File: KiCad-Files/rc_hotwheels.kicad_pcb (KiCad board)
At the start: 2 copper layers, 29.5 x 21.6 mm, 16 parts, among them IC1 BD6211F-E2, IC2 MIC5504-3.3YM5-TR, M1 Motor_Connection, U1 STM32F070F6P6, U3 NRF24L01_Breakout

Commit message: Merge branch 'master' of https://github.com/404boboo/RC-Hotwheels
Small changes in tracing
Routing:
- net Motor Speed: track 24.7 -> 24.2 mm
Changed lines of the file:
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@@
   (segment (start 61.39392 36.997797) (end 61.39392 39.72348) (width 0.4) (layer "F.Cu") (net 2))
   (segment (start 63.627 43.8856) (end 61.6458 43.8856) (width 0.4) (layer "F.Cu") (net 2))
+  (segment (start 62.743879 51.2262) (end 64.4906 51.2262) (width 0.4) (layer "F.Cu") (net 2))
   (segment (start 76.1238 35.2298) (end 71.058328 40.295272) (width 0.4) (layer "F.Cu") (net 2))
+  (segment (start 61.976 50.458321) (end 62.743879 51.2262) (width 0.4) (layer "F.Cu") (net 2))
   (segment (start 73.981636 48.110564) (end 76.7588 45.3334) (width 0.4) (layer "F.Cu") (net 2))
-  (segment (start 60.2742 44.7548) (end 61.4934 45.974) (width 0.4) (layer "F.Cu") (net 2))
+  (segment (start 61.976 46.4566) (end 61.976 50.458321) (width 0.4) (layer "F.Cu") (net 2))
   (segment (start 66.081593 44.170272) (end 63.911672 44.170272) (width 0.4) (layer "F.Cu") (net 2))
+  (segment (start 60.2742 44.7548) (end 61.976 46.4566) (width 0.4) (layer "F.Cu") (net 2))
   (segment (start 61.6458 43.8856) (end 60.3306 43.8856) (width 0.4) (layer "F.Cu") (net 2))
-  (segment (start 61.976 50.458321) (end 61.976 46.8122) (width 0.4) (layer "F.Cu") (net 2))
   (segment (start 64.4906 51.2262) (end 66.5378 51.2262) (width 0.4) (layer "F.Cu") (net 2))
   (segment (start 76.5048 35.2298) (end 76.1238 35.2298) (width 0.4) (layer "F.Cu") (net 2))
@@
   (segment (start 74.803 45.3334) (end 76.7588 45.3334) (width 0.4) (layer "F.Cu") (net 2))
   (segment (start 62.004364 48.110564) (end 73.981636 48.110564) (width 0.4) (layer "F.Cu") (net 2))
-  (segment (start 61.4934 45.974) (end 61.976 45.974) (width 0.4) (layer "F.Cu") (net 2))
   (segment (start 61.39392 39.72348) (end 60.2742 40.8432) (width 0.4) (layer "F.Cu") (net 2))
-  (segment (start 61.976 46.8122) (end 61.976 45.974) (width 0.4) (layer "F.Cu") (net 2))
   (segment (start 70.06 41.289679) (end 70.06 44.100544) (width 0.4) (layer "F.Cu") (net 2))
   (segment (start 69.990272 44.170272) (end 66.081593 44.170272) (width 0.4) (layer "F.Cu") (net 2))
@@
   (segment (start 71.054407 40.295272) (end 70.06 41.289679) (width 0.4) (layer "F.Cu") (net 2))
   (segment (start 63.911672 44.170272) (end 63.627 43.8856) (width 0.4) (layer "F.Cu") (net 2))
-  (segment (start 62.743879 51.2262) (end 61.976 50.458321) (width 0.4) (layer "F.Cu") (net 2))
-  (segment (start 64.4906 51.2262) (end 62.743879 51.2262) (width 0.4) (layer "F.Cu") (net 2))
   (segment (start 60.3306 43.8856) (end 60.2742 43.942) (width 0.4) (layer "F.Cu") (net 2))
   (segment (start 66.5378 51.2262) (end 66.588 51.176) (width 0.4) (layer "F.Cu") (net 2))
@@
   (segment (start 66.081593 39.14547) (end 66.081593 40.920272) (width 0.2) (layer "F.Cu") (net 13))
   (segment (start 65.22392 38.287797) (end 66.081593 39.14547) (width 0.2) (layer "F.Cu") (net 13))
+  (segment (start 67.76392 41.383102) (end 67.76392 38.287797) (width 0.2) (layer "F.Cu") (net 14))
+  (segment (start 67.57675 41.570272) (end 67.76392 41.383102) (width 0.2) (layer "F.Cu") (net 14))
   (segment (start 66.081593 41.570272) (end 67.57675 41.570272) (width 0.2) (layer "F.Cu") (net 14))
-  (segment (start 67.57675 41.570272) (end 67.76392 41.383102) (width 0.2) (layer "F.Cu") (net 14))
-  (segment (start 67.76392 41.383102) (end 67.76392 38.287797) (width 0.2) (layer "F.Cu") (net 14))
   (segment (start 65.044093 41.015693) (end 65.044093 41.919536) (width 0.2) (layer "F.Cu") (net 15))
   (segment (start 65.344829 42.220272) (end 66.081593 42.220272) (width 0.2) (layer "F.Cu") (net 15))
@@
   (segment (start 65.22392 35.747797) (end 64.008 36.963717) (width 0.2) (layer "F.Cu") (net 15))
   (segment (start 65.044093 41.919536) (end 65.344829 42.220272) (width 0.2) (layer "F.Cu") (net 15))
-  (segment (start 68.355529 42.19) (end 67.845529 42.7) (width 0.2) (layer "F.Cu") (net 18))
-  (segment (start 71.4248 37.96788) (end 68.355529 41.037151) (width 0.2) (layer "F.Cu") (net 18))
+  (segment (start 68.8605 41.685029) (end 67.845529 42.7) (width 0.2) (layer "F.Cu") (net 18))
+  (segment (start 68.8605 40.532181) (end 68.8605 41.685029) (width 0.2) (layer "F.Cu") (net 18))
+  (segment (start 71.4248 37.96788) (end 68.8605 40.532181) (width 0.2) (layer "F.Cu") (net 18))
+  (segment (start 68.289728 46.120272) (end 66.081593 46.120272) (width 0.2) (layer "F.Cu") (net 18))
+  (segment (start 71.4248 35.2298) (end 71.4248 37.96788) (width 0.2) (layer "F.Cu") (net 18))
   (segment (start 67.845529 42.7) (end 67.8 42.7) (width 0.2) (layer "F.Cu") (net 18))
-  (segment (start 68.289728 46.120272) (end 66.081593 46.120272) (width 0.2) (layer "F.Cu") (net 18))
-  (segment (start 68.355529 41.037151) (end 68.355529 42.19) (width 0.2) (layer "F.Cu") (net 18))
   (segment (start 68.72 45.69) (end 68.289728 46.120272) (width 0.2) (layer "F.Cu") (net 18))
-  (segment (start 71.4248 35.2298) (end 71.4248 37.96788) (width 0.2) (layer "F.Cu") (net 18))
   (via (at 68.72 45.69) (size 0.8) (drill 0.4) (layers "F.Cu" "B.Cu") (net 18))
   (via (at 67.8 42.7) (size 0.8) (drill 0.4) (layers "F.Cu" "B.Cu") (net 18))
@@
   (segment (start 67.8 42.7) (end 67.8 44.77) (width 0.2) (layer "B.Cu") (net 18))
   (segment (start 73.9648 35.2298) (end 73.9648 35.993566) (width 0.2) (layer "F.Cu") (net 19))
-  (segment (start 73.9648 35.993566) (end 68.755529 41.202837) (width 0.2) (layer "F.Cu") (net 19))
-  (segment (start 68.755529 41.202837) (end 68.755529 42.364471) (width 0.2) (layer "F.Cu") (net 19))
+  (segment (start 73.9648 35.993566) (end 69.2605 40.697866) (width 0.2) (layer "F.Cu") (net 19))
   (segment (start 69.219728 46.770272) (end 66.081593 46.770272) (width 0.2) (layer "F.Cu") (net 19))
-  (segment (start 68.755529 42.364471) (end 69.231058 42.84) (width 0.2) (layer "F.Cu") (net 19))
-  (segment (start 69.231058 42.84) (end 69.2605 42.84) (width 0.2) (layer "F.Cu") (net 19))
+  (segment (start 69.2605 40.697866) (end 69.2605 42.84) (width 0.2) (layer "F.Cu") (net 19))
   (segment (start 69.71 46.28) (end 69.219728 46.770272) (width 0.2) (layer "F.Cu") (net 19))
   (via (at 69.71 46.28) (size 0.8) (drill 0.4) (layers "F.Cu" "B.Cu") (net 19))
@@
   (segment (start 65.202951 54.5338) (end 60.046751 49.3776) (width 0.4) (layer "F.Cu") (net 20))
   (segment (start 70.9422 51.658) (end 70.9422 54.356) (width 0.4) (layer "F.Cu") (net 20))
+  (segment (start 77.948391 37.901009) (end 77.948391 51.369988) (width 0.4) (layer "F.Cu") (net 20))
   (segment (start 81.8896 38.6842) (end 81.8896 37.2618) (width 0.4) (layer "F.Cu") (net 20))
   (segment (start 81.7372 37.1094) (end 79.7198 37.1094) (width 0.4) (layer "F.Cu") (net 20))
   (segment (start 76.246392 54.5338) (end 71.12 54.5338) (width 0.4) (layer "F.Cu") (net 20))
-  (segment (start 79.7198 37.1094) (end 78.045782 37.1094) (width 0.4) (layer "F.Cu") (net 20))
-  (segment (start 78.045782 37.1094) (end 77.948391 37.206791) (width 0.4) (layer "F.Cu") (net 20))
   (segment (start 77.443517 53.336675) (end 76.246392 54.5338) (width 0.4) (layer "F.Cu") (net 20))
   (segment (start 69.088 51.176) (end 70.4602 51.176) (width 0.4) (layer "F.Cu") (net 20))
-  (segment (start 77.443517 51.874862) (end 77.948391 51.369988) (width 0.4) (layer "F.Cu") (net 20))
   (segment (start 81.8896 37.2618) (end 81.7372 37.1094) (width 0.4) (layer "F.Cu") (net 20))
   (segment (start 79.7198 37.1094) (end 80.6196 38.0092) (width 0.4) (layer "F.Cu") (net 20))
@@
   (segment (start 77.443517 51.874862) (end 77.443517 53.336675) (width 0.4) (layer "F.Cu") (net 20))
   (segment (start 60.046751 49.3776) (end 59.7916 49.3776) (width 0.4) (layer "F.Cu") (net 20))
-  (segment (start 77.948391 37.206791) (end 77.948391 51.369988) (width 0.4) (layer "F.Cu") (net 20))
+  (segment (start 77.948391 51.369988) (end 77.443517 51.874862) (width 0.4) (layer "F.Cu") (net 20))
+  (segment (start 78.74 37.1094) (end 77.948391 37.901009) (width 0.4) (layer "F.Cu") (net 20))
   (segment (start 70.9422 54.356) (end 71.12 54.5338) (width 0.4) (layer "F.Cu") (net 20))
+  (segment (start 79.7198 37.1094) (end 78.74 37.1094) (width 0.4) (layer "F.Cu") (net 20))
   (segment (start 80.6196 38.0092) (end 80.6196 38.6842) (width 0.4) (layer "F.Cu") (net 20))
   (segment (start 71.12 54.5338) (end 65.202951 54.5338) (width 0.4) (layer "F.Cu") (net 20))
@@
   (segment (start 76.806344 41.613585) (end 79.108428 41.613585) (width 0.2) (layer "B.Cu") (net 23))
   (segment (start 76.247654 41.054895) (end 76.806344 41.613585) (width 0.2) (layer "B.Cu") (net 23))
-  (segment (start 63.5 46.736) (end 63.5 45.490695) (width 0.2) (layer "F.Cu") (net 24))
-  (segment (start 63.585989 45.404706) (end 64.216575 45.404706) (width 0.2) (layer "F.Cu") (net 24))
+  (segment (start 65.116303 44.820272) (end 66.081593 44.820272) (width 0.2) (layer "F.Cu") (net 24))
+  (segment (start 63.5 46.736) (end 63.5 46.436575) (width 0.2) (layer "F.Cu") (net 24))
   (segment (start 80.6196 47.5742) (end 80.6196 44.5842) (width 0.2) (layer "F.Cu") (net 24))
-  (segment (start 64.216575 45.404706) (end 64.801009 44.820272) (width 0.2) (layer "F.Cu") (net 24))
-  (segment (start 64.801009 44.820272) (end 66.081593 44.820272) (width 0.2) (layer "F.Cu") (net 24))
-  (segment (start 63.5 45.490695) (end 63.585989 45.404706) (width 0.2) (layer "F.Cu") (net 24))
+  (segment (start 63.5 46.436575) (end 65.116303 44.820272) (width 0.2) (layer "F.Cu") (net 24))
   (via (at 63.5 46.736) (size 0.8) (drill 0.4) (layers "F.Cu" "B.Cu") (net 24))
   (via (at 80.6196 47.5742) (size 0.8) (drill 0.4) (layers "F.Cu" "B.Cu") (net 24))
@@
         (xy 78.062836 37.182265)
         (xy 78.256311 47.081751)
-        (xy 84.22793 47.006512)
+        (xy 84.189554 46.85603)
         (xy 84.157308 37.182265)
         (xy 78.03059 37.214511)

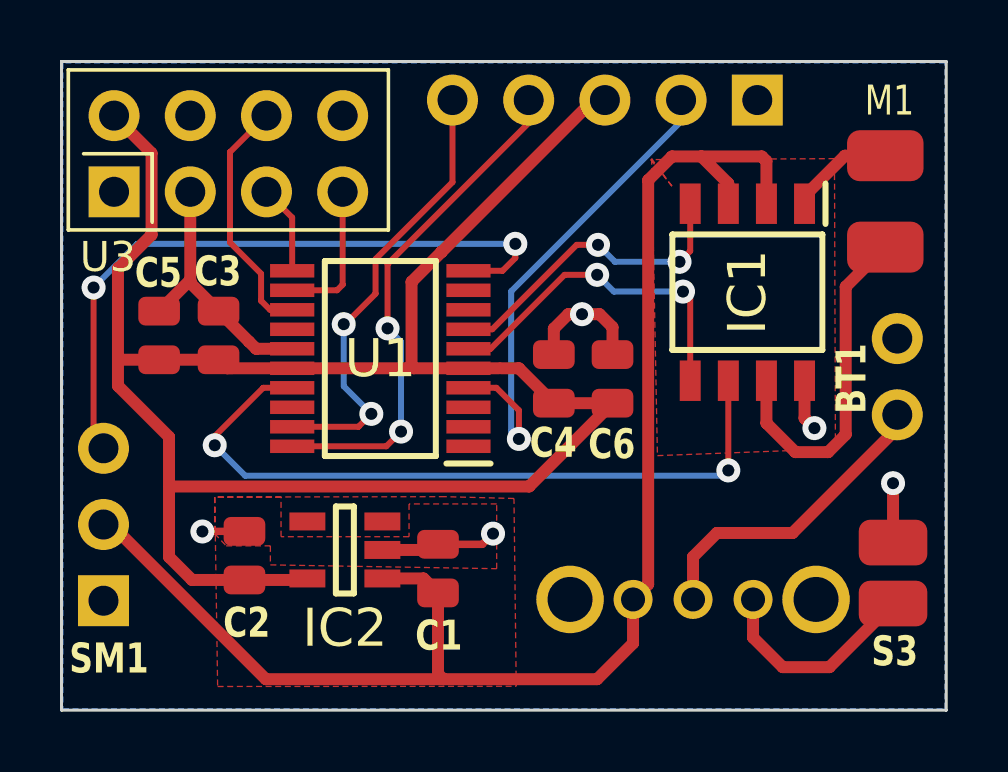
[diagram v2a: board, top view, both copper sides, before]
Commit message: Changed Radio Receiver to Bluetooth Module
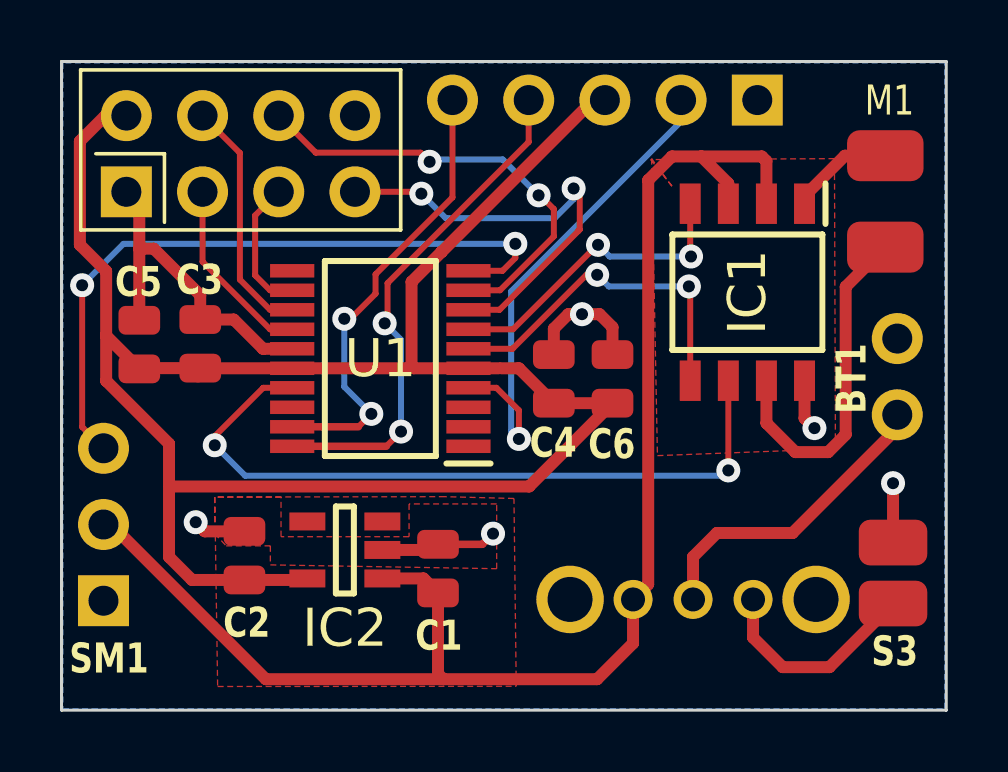
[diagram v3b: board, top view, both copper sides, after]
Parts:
- U3: value NRF24L01_Breakout -> HM-BT4502
- moved C5 0.73 mm to (61.0, 43.4)
- moved C3 0.67 mm to (63.0, 43.4)
- moved U3 0.41 mm to (60.6, 38.3)
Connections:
- U1 pad 11: SCK -> unconnected-(U1A-PA5-Pad11)
- U1 pad 12: MISO -> PND
- U1 pad 13: MOSI -> INT
- U1 pad 14: unconnected-(U1A-PB1-Pad14) -> WAKEUP
- U1 pad 8: unconnected-(U1A-PA2-Pad8) -> RXD
- U1 pad 9: unconnected-(U1A-PA3-Pad9) -> TXD
- U3 pad 3: GND -> WAKEUP
- U3 pad 4: GND -> INT
- U3 pad 5: SCK -> PND
- U3 pad 6: MOSI -> TXD
- U3 pad 7: MISO -> RXD
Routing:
- net TXD: track 0.00 -> 15.0 mm, vias 0 -> 2
- net RXD: track 0.00 -> 14.8 mm, vias 0 -> 2
- net MOSI: track 8.27 -> 0.00 mm
- net INT: track 0.00 -> 8.14 mm
- net WAKEUP: track 0.00 -> 6.99 mm
- net MISO: track 4.86 -> 0.00 mm
- net PND: track 0.00 -> 4.55 mm
- net GND: track 21.9 -> 24.9 mm
- net SCK: track 2.99 -> 0.00 mm
- net VR_OUT: track 66.1 -> 67.6 mm
- net PWM: track 22.4 -> 23.0 mm
